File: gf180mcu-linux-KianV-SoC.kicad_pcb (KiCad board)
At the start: 4 copper layers, 94.7 x 52.4 mm, 65 parts, among them CN1 Conn_02x35_Counter_Clockwise, J2 Conn_01x06_Pin, J3 Conn_01x06_Pin, J4 Conn_02x06_Top_Bottom_custom, J5 USB_C_Receptacle_PowerOnly_6P, SW1 SW_Push, U1 MT48LC16M16A2P, U2 TPS3808DBV, U3 TLV62569DBV, U4 503398-1892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

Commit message: remove drc warnings, added machdyne credit
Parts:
- removed REF**: HR, hrvatski_proizvod_veci:hrvatski
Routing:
- net /3V3: track 442.8 -> 442.7 mm, vias 35 -> 33
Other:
- board text added: "Board design by Goran Maholvic, Andrew Wingate, Philip Lalone, Hirosh Dabui"
- board text removed: "Board design by Goran Maholvic & Andrew Wingate"

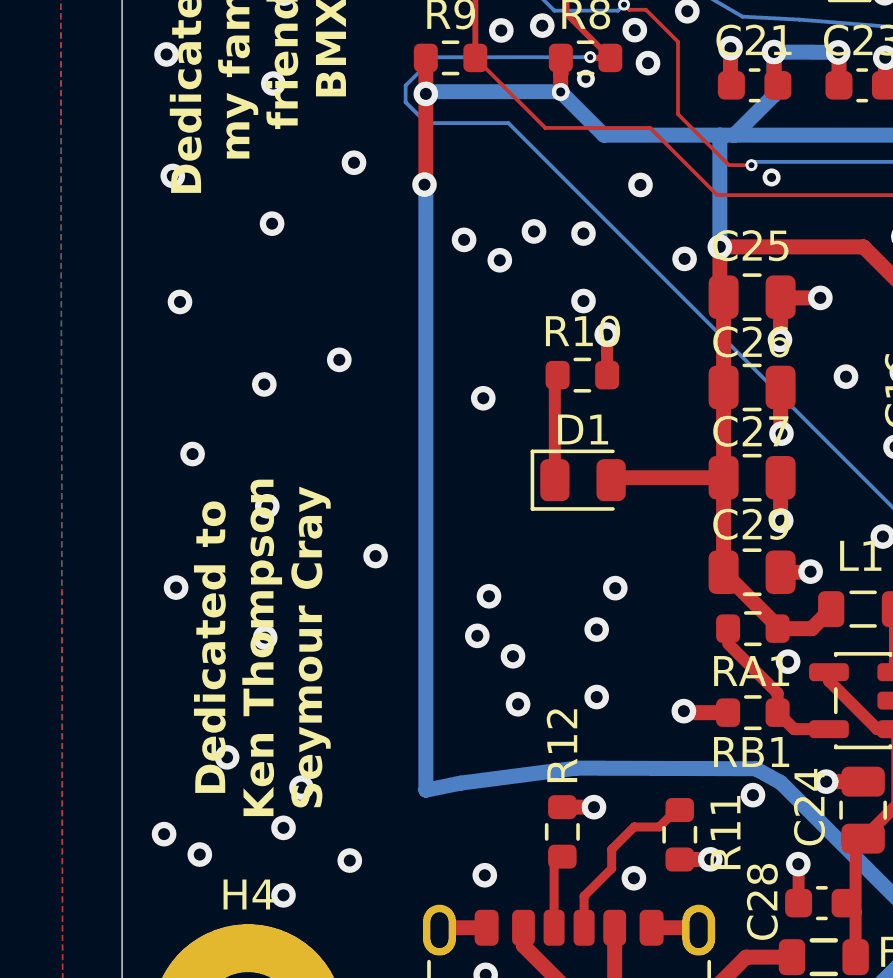
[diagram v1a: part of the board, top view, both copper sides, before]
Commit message: rounded vcc signal
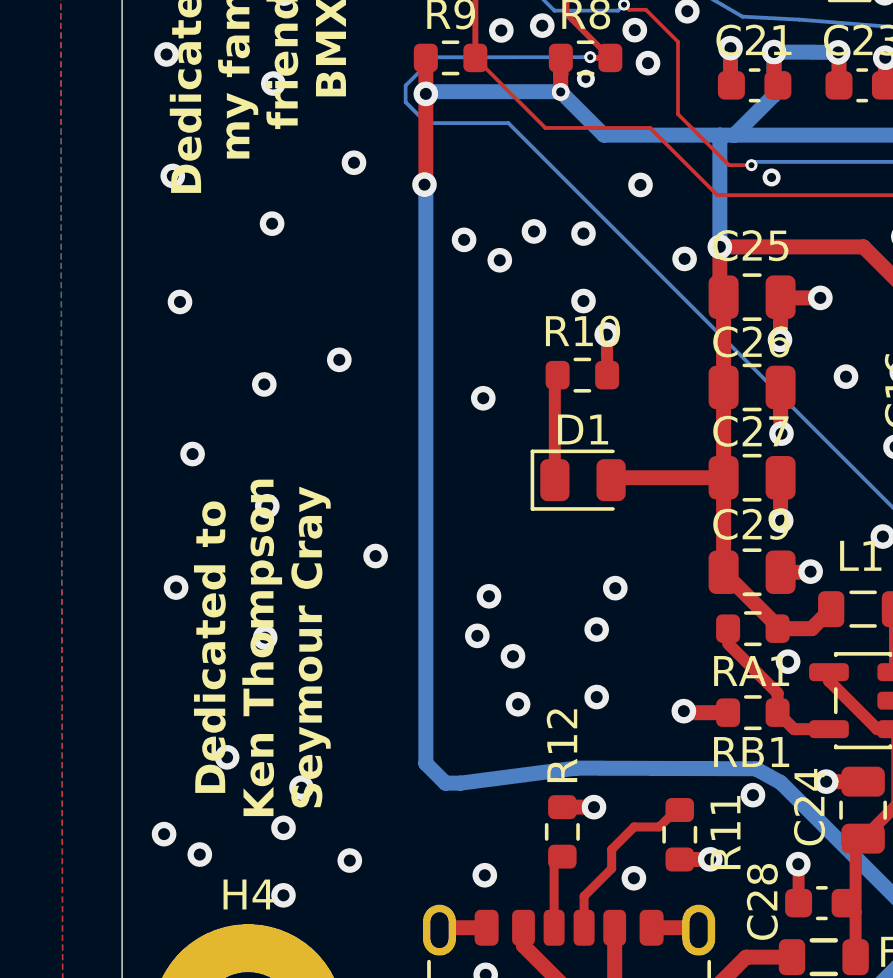
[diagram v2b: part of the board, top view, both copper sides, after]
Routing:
- net /3V3: track 442.7 -> 442.0 mm
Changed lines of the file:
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@@
+	)
+	(segment
+		(start 157.38 229)
+		(end 157.38 226.78)
+		(width 0.5)
+		(layer "B.Cu")
+		(net "/3V3")
 	)
 	(segment
@@
 	)
 	(segment
+		(start 158.38 224.406928)
+		(end 154.052072 220.079)
+		(width 0.5)
+		(layer "B.Cu")
+		(net "/3V3")
+	)
+	(segment
 		(start 188.03 211.4)
 		(end 189.105 212.475)
@@
 	)
 	(segment
-		(start 158.38 225.78)
-		(end 158.38 224.406928)
+		(start 157.38 226.78)
+		(end 158.38 225.78)
 		(width 0.5)
 		(layer "B.Cu")
@@
 	)
 	(segment
-		(start 157.38 226.78)
-		(end 158.38 225.78)
-		(width 0.5)
-		(layer "B.Cu")
-		(net "/3V3")
-	)
-	(segment
 		(start 158.875 198.5)
 		(end 152.5 198.5)
@@
 	)
 	(segment
+		(start 164.83 227.7)
+		(end 164.78 227.75)
+		(width 0.5)
+		(layer "B.Cu")
+		(net "/3V3")
+	)
+	(segment
+		(start 202.82 200.51)
+		(end 203.36 201.05)
+		(width 0.5)
+		(layer "B.Cu")
+		(net "/3V3")
+	)
+	(segment
+		(start 195.32 225.32)
+		(end 195.33 225.33)
+		(width 0.5)
+		(layer "B.Cu")
+		(net "/3V3")
+	)
+	(segment
+		(start 178.58 203.025)
+		(end 176.88 203.025)
+		(width 0.5)
+		(layer "B.Cu")
+		(net "/3V3")
+	)
+	(segment
+		(start 198.23 194.46)
+		(end 198.35 200.99)
+		(width 0.5)
+		(layer "B.Cu")
+		(net "/3V3")
+	)
+	(segment
+		(start 215.25 224.17)
+		(end 214.09 225.33)
+		(width 0.5)
+		(layer "B.Cu")
+		(net "/3V3")
+	)
+	(segment
 		(start 154.052072 220.079)
 		(end 153.22 219.62)
@@
 	)
 	(segment
-		(start 164.83 227.7)
-		(end 164.78 227.75)
-		(width 0.5)
-		(layer "B.Cu")
-		(net "/3V3")
-	)
-	(segment
-		(start 202.82 200.51)
-		(end 203.36 201.05)
-		(width 0.5)
-		(layer "B.Cu")
-		(net "/3V3")
-	)
-	(segment
-		(start 195.32 225.32)
-		(end 195.33 225.33)
-		(width 0.5)
-		(layer "B.Cu")
-		(net "/3V3")
-	)
-	(segment
-		(start 178.58 203.025)
-		(end 176.88 203.025)
-		(width 0.5)
-		(layer "B.Cu")
-		(net "/3V3")
-	)
-	(segment
-		(start 198.23 194.46)
-		(end 198.35 200.99)
-		(width 0.5)
-		(layer "B.Cu")
-		(net "/3V3")
-	)
-	(segment
-		(start 215.25 224.17)
-		(end 214.09 225.33)
-		(width 0.5)
-		(layer "B.Cu")
-		(net "/3V3")
-	)
-	(segment
-		(start 157.38 229)
-		(end 157.38 226.78)
-		(width 0.5)
-		(layer "B.Cu")
-		(net "/3V3")
-	)
-	(segment
 		(start 209.64 194.46)
 		(end 209.64 197.1)
@@
 		(start 195.305 225.305)
 		(end 195.32 225.32)
+		(width 0.5)
+		(layer "B.Cu")
+		(net "/3V3")
+	)
+	(segment
+		(start 153.22 219.62)
+		(end 147.232 219.6)
 		(width 0.5)
 		(layer "B.Cu")
@@
 	)
 	(segment
+		(start 142.225 200.245)
+		(end 142.13 200.15)
+		(width 0.5)
+		(layer "B.Cu")
+		(net "/3V3")
+	)
+	(segment
 		(start 181.13 209.575)
 		(end 181.13 208.6)
@@
 	)
 	(segment
-		(start 142.225 200.245)
-		(end 142.13 200.15)
-		(width 0.5)
-		(layer "B.Cu")
-		(net "/3V3")
-	)
-	(segment
-		(start 147.232 219.6)
-		(end 143.38 220.1)
-		(width 0.5)
-		(layer "B.Cu")
-		(net "/3V3")
-	)
-	(segment
 		(start 189.055 208.05)
 		(end 187.705 208.05)
@@
 	)
 	(segment
+		(start 166.18 230.85)
+		(end 159.23 230.85)
+		(width 0.5)
+		(layer "B.Cu")
+		(net "/3V3")
+	)
+	(segment
 		(start 146.71 197.05)
 		(end 148.16 198.5)
@@
 	)
 	(segment
+		(start 143.38 220.1)
+		(end 142.88 220.1)
+		(width 0.5)
+		(layer "B.Cu")
+		(net "/3V3")
+	)
+	(segment
 		(start 153.83 195.73)
 		(end 155.97 195.74)
@@
 	)
 	(segment
-		(start 159.23 230.85)
-		(end 157.38 229)
+		(start 158.38 225.78)
+		(end 158.38 224.406928)
 		(width 0.5)
 		(layer "B.Cu")
@@
 	)
 	(segment
-		(start 158.38 224.406928)
-		(end 154.052072 220.079)
-		(width 0.5)
-		(layer "B.Cu")
-		(net "/3V3")
-	)
-	(segment
 		(start 200.505 225.33)
 		(end 201.43 225.33)
@@
 	)
 	(segment
+		(start 142.225 219.445)
+		(end 142.225 200.245)
+		(width 0.5)
+		(layer "B.Cu")
+		(net "/3V3")
+	)
+	(segment
 		(start 174.685 192.54)
 		(end 173.63 192.54)
-		(width 0.5)
-		(layer "B.Cu")
-		(net "/3V3")
-	)
-	(segment
-		(start 143.38 220.1)
-		(end 142.225 220.335)
 		(width 0.5)
 		(layer "B.Cu")
@@
 	)
 	(segment
-		(start 153.22 219.62)
-		(end 147.232 219.6)
-		(width 0.5)
-		(layer "B.Cu")
-		(net "/3V3")
-	)
-	(segment
-		(start 142.225 220.335)
-		(end 142.225 200.245)
+		(start 159.23 230.85)
+		(end 157.38 229)
 		(width 0.5)
 		(layer "B.Cu")
@@
 	)
 	(segment
+		(start 142.88 220.1)
+		(end 142.225 219.445)
+		(width 0.5)
+		(layer "B.Cu")
+		(net "/3V3")
+	)
+	(segment
+		(start 147.232 219.6)
+		(end 143.38 220.1)
+		(width 0.5)
+		(layer "B.Cu")
+		(net "/3V3")
+	)
+	(segment
 		(start 205.18 225.33)
 		(end 206.11 225.33)
@@
 		(width 0.5)
 		(layer "B.Cu")
-		(net "/3V3")
-	)
-	(segment
-		(start 166.18 230.85)
-		(end 159.23 230.85)
-		(width 0.5)
-		(layer "B.Cu")

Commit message: Set C24 to 4.7uF
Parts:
- C24: value 22uF -> 4.7uF
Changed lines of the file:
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@@
 			)
 		)
-		(property "Value" "22uF"
+		(property "Value" "4.7uF"
 			(at 0 1.68 90)
 			(layer "F.Fab")
@@
 					(thickness 0.15)
 				)
-			)
-		)
-		(property "MPN" "CC0805ZKY5V5BB226 "
-			(at 0 0 90)
-			(unlocked yes)
-			(layer "F.Fab")
-			(hide yes)
-			(effects
-				(font
-					(size 1 1)
-					(thickness 0.15)
-				)
